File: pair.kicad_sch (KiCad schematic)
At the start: 1 part, among them U10 VNLD5090

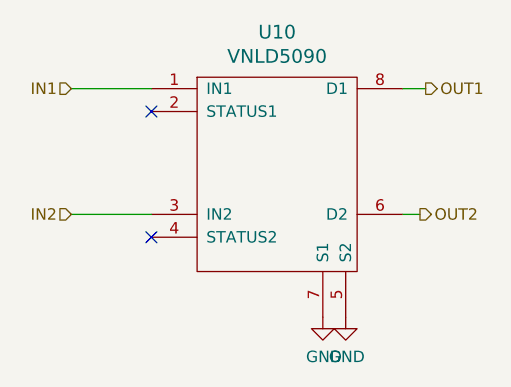
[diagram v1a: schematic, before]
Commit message: widened usb trace to further reduce impedence
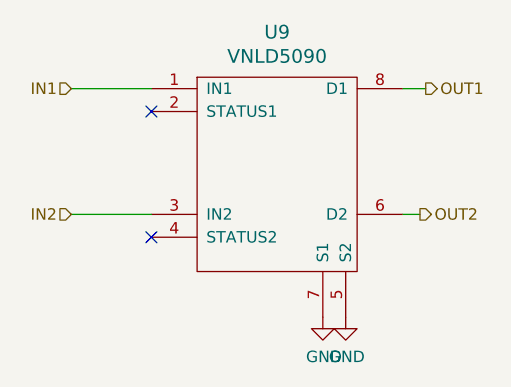
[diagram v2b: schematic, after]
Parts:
- renumbered U10 to U9
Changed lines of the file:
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@@
 		(on_board yes)
 		(dnp no)
-		(property "Reference" "U10"
+		(property "Reference" "U9"
 			(at 78.74 31.8262 0)
 			(effects
@@
 		(on_board yes)
 		(dnp no)
-		(property "Reference" "#PWR036"
+		(property "Reference" "#PWR030"
 			(at 83.82 69.85 0)
 			(effects
@@
 		(on_board yes)
 		(dnp no)
-		(property "Reference" "#PWR037"
+		(property "Reference" "#PWR031"
 			(at 86.36 69.85 0)
 			(effects
